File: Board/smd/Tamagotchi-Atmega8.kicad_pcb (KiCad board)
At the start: 2 copper layers, 47.8 x 47.8 mm, 27 parts, among them J1 Conn_02x05_Odd_Even, J2 Conn_01x02, J3 Conn_01x04, J4 Conn_01x07, J5 Conn_01x02, Q1 Q_NPN_BEC, SW1 SW_Push, U1 AMS1117, U2 ATmega328-AU, U3 DS1307Z+, X1 8MHz, X2 32768kHz

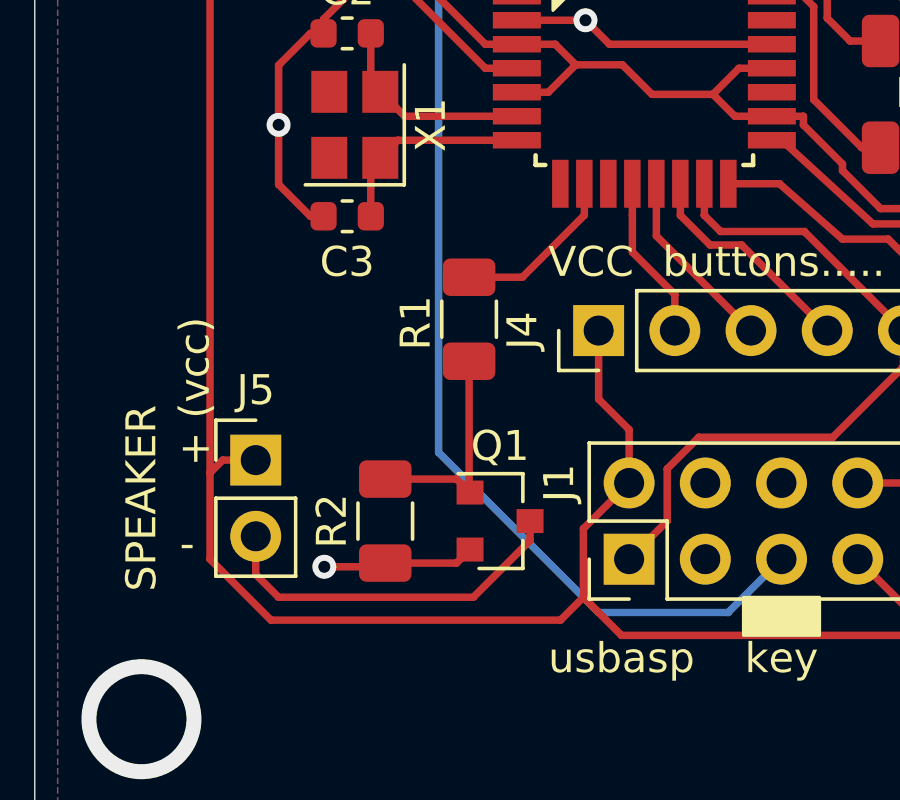
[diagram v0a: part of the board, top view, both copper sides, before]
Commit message: fixed buttons polarity (pull-up state and negative activation)
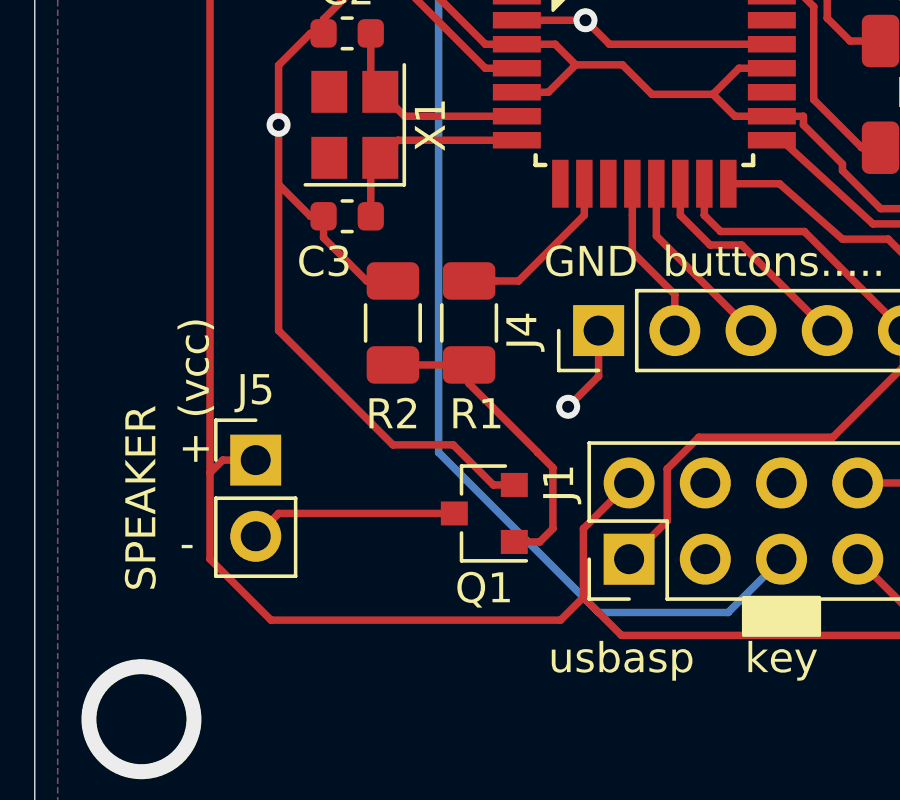
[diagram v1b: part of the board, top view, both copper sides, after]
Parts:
- moved R2 6.61 mm to (118.9, 94.7), turned to 90 degrees
- moved Q1 0.58 mm to (121.9, 101.1), turned to 180 degrees
- moved R1 0.12 mm to (121.4, 94.7)
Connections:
- J4 pad 1: VCC -> GND
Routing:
- net GND: track 90.1 -> 106.4 mm
- net VCC: track 183.7 -> 178.2 mm
- net Net-(J5-Pad2): track 12.2 -> 6.94 mm
- net Net-(Q1-Pad1): track 7.40 -> 10.6 mm
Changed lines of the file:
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@@
     (thickness 1.6)
     (drawings 22)
-    (tracks 258)
+    (tracks 263)
     (zones 0)
     (modules 27)
@@
       (net 16 "Net-(J4-Pad2)"))
     (pad 1 thru_hole rect (at 0 0 90) (size 1.7 1.7) (drill 1) (layers *.Cu *.Mask)
-      (net 2 VCC))
+      (net 1 GND))
     (model ${KISYS3DMOD}/Connector_PinHeader_2.54mm.3dshapes/PinHeader_1x07_P2.54mm_Vertical.wrl
       (at (xyz 0 0 0))
@@
   )
   (module Resistor_SMD:R_1206_3216Metric (layer F.Cu)
-    (at 118.618 101.346 270)
+    (at 118.872 94.742 90)
     (descr "Resistor SMD 1206 (3216 Metric), square (rectangular) end terminal, IPC_7351 nominal, (Body size source: http://www.tortai-tech.com/upload/download/2011102023233369053.pdf), generated with kicad-footprint-generator")
     (tags resistor)
     (attr smd)
-    (fp_text reference R2 (at 0 1.778 90) (layer F.SilkS)
+    (fp_text reference R2 (at -3.048 0 180) (layer F.SilkS)
       (effects (font (size 1 1) (thickness 0.15)))
     )
@@
     (fp_line (start -1.6 -0.8) (end 1.6 -0.8) (layer F.Fab) (width 0.1))
     (fp_line (start -1.6 0.8) (end -1.6 -0.8) (layer F.Fab) (width 0.1))
-    (pad 2 smd roundrect (at 1.4 0 270) (size 1.25 1.75) (layers F.Cu F.Paste F.Mask) (roundrect_rratio 0.2)
-      (net 1 GND))
-    (pad 1 smd roundrect (at -1.4 0 270) (size 1.25 1.75) (layers F.Cu F.Paste F.Mask) (roundrect_rratio 0.2)
+    (pad 2 smd roundrect (at 1.4 0 90) (size 1.25 1.75) (layers F.Cu F.Paste F.Mask) (roundrect_rratio 0.2)
+      (net 1 GND))
+    (pad 1 smd roundrect (at -1.4 0 90) (size 1.25 1.75) (layers F.Cu F.Paste F.Mask) (roundrect_rratio 0.2)
       (net 21 "Net-(Q1-Pad1)"))
     (model ${KISYS3DMOD}/Resistor_SMD.3dshapes/R_1206_3216Metric.wrl
@@
   )
   (module Resistor_SMD:R_1206_3216Metric (layer F.Cu)
-    (at 121.412 94.618 270)
+    (at 121.412 94.742 270)
     (descr "Resistor SMD 1206 (3216 Metric), square (rectangular) end terminal, IPC_7351 nominal, (Body size source: http://www.tortai-tech.com/upload/download/2011102023233369053.pdf), generated with kicad-footprint-generator")
     (tags resistor)
     (attr smd)
-    (fp_text reference R1 (at 0.124 1.778 90) (layer F.SilkS)
+    (fp_text reference R1 (at 3.048 -0.254 180) (layer F.SilkS)
       (effects (font (size 1 1) (thickness 0.15)))
     )
@@
   )
   (module Package_TO_SOT_SMD:SOT-23 (layer F.Cu)
-    (at 122.444 101.346)
+    (at 121.92 101.092 180)
     (descr "SOT-23, Standard")
     (tags SOT-23)
@@
       (effects (font (size 0.5 0.5) (thickness 0.075)))
     )
-    (pad 3 smd rect (at 1 0) (size 0.9 0.8) (layers F.Cu F.Paste F.Mask)
+    (pad 3 smd rect (at 1 0 180) (size 0.9 0.8) (layers F.Cu F.Paste F.Mask)
       (net 17 "Net-(J5-Pad2)"))
-    (pad 2 smd rect (at -1 0.95) (size 0.9 0.8) (layers F.Cu F.Paste F.Mask)
-      (net 1 GND))
-    (pad 1 smd rect (at -1 -0.95) (size 0.9 0.8) (layers F.Cu F.Paste F.Mask)
+    (pad 2 smd rect (at -1 0.95 180) (size 0.9 0.8) (layers F.Cu F.Paste F.Mask)
+      (net 1 GND))
+    (pad 1 smd rect (at -1 -0.95 180) (size 0.9 0.8) (layers F.Cu F.Paste F.Mask)
       (net 21 "Net-(Q1-Pad1)"))
     (model ${KISYS3DMOD}/Package_TO_SOT_SMD.3dshapes/SOT-23.wrl
@@
     (tags capacitor)
     (attr smd)
-    (fp_text reference C3 (at 0 1.524) (layer F.SilkS)
+    (fp_text reference C3 (at -0.762 1.524) (layer F.SilkS)
       (effects (font (size 1 1) (thickness 0.15)))
     )
@@
     (effects (font (size 1 1) (thickness 0.15)))
   )
-  (gr_text VCC (at 125.476 92.71) (layer F.SilkS)
+  (gr_text GND (at 125.476 92.71) (layer F.SilkS)
     (effects (font (size 1 1) (thickness 0.15)))
   )
@@
   (via (at 110.49 107.95) (size 4) (drill 3) (layers F.Cu B.Cu) (net 1))
   (via (at 110.49 67.31) (size 4) (drill 3) (layers F.Cu B.Cu) (net 1))
-  (segment (start 120.994 102.746) (end 121.444 102.296) (width 0.25) (layer F.Cu) (net 1))
-  (segment (start 118.618 102.746) (end 120.994 102.746) (width 0.25) (layer F.Cu) (net 1))
   (segment (start 147.658 70.358) (end 146.558 70.358) (width 0.25) (layer F.Cu) (net 1))
   (segment (start 148.59 80.264) (end 148.59 71.29) (width 0.25) (layer F.Cu) (net 1))
@@
   (segment (start 125.292 84.652) (end 125.292 84.652) (width 0.25) (layer F.Cu) (net 1))
   (via (at 125.292 84.652) (size 0.8) (drill 0.4) (layers F.Cu B.Cu) (net 1))
-  (via (at 116.586 102.87) (size 0.8) (drill 0.4) (layers F.Cu B.Cu) (net 1))
+  (via (at 124.714 97.536) (size 0.8) (drill 0.4) (layers F.Cu B.Cu) (net 1))
   (segment (start 144.866 96.688) (end 144.866 101.578) (width 0.25) (layer F.Cu) (net 1))
   (via (at 144.866 101.6) (size 0.8) (drill 0.4) (layers F.Cu B.Cu) (net 1))
@@
   (via (at 129.794 76.962) (size 0.8) (drill 0.4) (layers F.Cu B.Cu) (net 1))
   (segment (start 128.548 78.359) (end 129.794 77.113) (width 0.25) (layer F.Cu) (net 1))
-  (segment (start 118.494 102.87) (end 118.618 102.746) (width 0.25) (layer F.Cu) (net 1))
-  (segment (start 116.586 102.87) (end 118.494 102.87) (width 0.25) (layer F.Cu) (net 1))
+  (segment (start 117.997 93.342) (end 118.872 93.342) (width 0.25) (layer F.Cu) (net 1))
+  (segment (start 116.5605 91.9055) (end 117.997 93.342) (width 0.25) (layer F.Cu) (net 1))
+  (segment (start 116.5605 91.186) (end 116.5605 91.9055) (width 0.25) (layer F.Cu) (net 1))
+  (segment (start 122.22 100.142) (end 120.884 98.806) (width 0.25) (layer F.Cu) (net 1))
+  (segment (start 122.92 100.142) (end 122.22 100.142) (width 0.25) (layer F.Cu) (net 1))
+  (segment (start 120.884 98.806) (end 118.872 98.806) (width 0.25) (layer F.Cu) (net 1))
+  (segment (start 115.062 94.996) (end 115.062 90.125) (width 0.25) (layer F.Cu) (net 1))
+  (segment (start 118.872 98.806) (end 115.062 94.996) (width 0.25) (layer F.Cu) (net 1))
+  (segment (start 125.73 96.52) (end 124.714 97.536) (width 0.25) (layer F.Cu) (net 1))
+  (segment (start 125.73 94.996) (end 125.73 96.52) (width 0.25) (layer F.Cu) (net 1))
   (segment (start 136.646 72.898) (end 136.652 72.892) (width 0.25) (layer F.Cu) (net 2))
   (segment (start 149.266 101.006) (end 149.18 101.092) (width 0.25) (layer F.Cu) (net 2))
@@
   (segment (start 148.59 105.156) (end 149.255001 104.490999) (width 0.25) (layer F.Cu) (net 2))
   (segment (start 123.004 85.452) (end 121.954 85.452) (width 0.25) (layer F.Cu) (net 2))
-  (segment (start 126.746 100.076) (end 126.746 98.298) (width 0.25) (layer F.Cu) (net 2))
-  (segment (start 125.73 97.282) (end 125.73 94.996) (width 0.25) (layer F.Cu) (net 2))
-  (segment (start 126.746 98.298) (end 125.73 97.282) (width 0.25) (layer F.Cu) (net 2))
   (segment (start 141.63 98.942) (end 141.63 101.092) (width 0.25) (layer F.Cu) (net 2))
   (segment (start 132.556 87.852) (end 132.556 88.14119) (width 0.25) (layer F.Cu) (net 2))
@@
   (segment (start 128.27 93.793919) (end 126.854 92.377919) (width 0.25) (layer F.Cu) (net 16))
   (segment (start 128.27 94.996) (end 128.27 93.793919) (width 0.25) (layer F.Cu) (net 16))
-  (segment (start 115.062 103.886) (end 114.3 103.124) (width 0.25) (layer F.Cu) (net 17))
-  (segment (start 121.554 103.886) (end 115.062 103.886) (width 0.25) (layer F.Cu) (net 17))
-  (segment (start 114.3 103.124) (end 114.3 101.854) (width 0.25) (layer F.Cu) (net 17))
-  (segment (start 123.444 101.346) (end 123.444 101.996) (width 0.25) (layer F.Cu) (net 17))
-  (segment (start 123.444 101.996) (end 121.554 103.886) (width 0.25) (layer F.Cu) (net 17))
+  (segment (start 115.062 101.092) (end 114.3 101.854) (width 0.25) (layer F.Cu) (net 17))
+  (segment (start 120.92 101.092) (end 115.062 101.092) (width 0.25) (layer F.Cu) (net 17))
   (segment (start 139.44 88.9) (end 140.202 89.662) (width 0.25) (layer F.Cu) (net 18))
   (segment (start 137.928 88.9) (end 139.44 88.9) (width 0.25) (layer F.Cu) (net 18))
@@
   (segment (start 139.44 81.788) (end 140.202 81.026) (width 0.25) (layer F.Cu) (net 20))
   (segment (start 137.922 81.788) (end 139.44 81.788) (width 0.25) (layer F.Cu) (net 20))
-  (segment (start 121.412 100.364) (end 121.444 100.396) (width 0.25) (layer F.Cu) (net 21))
-  (segment (start 121.412 96.018) (end 121.412 100.364) (width 0.25) (layer F.Cu) (net 21))
-  (segment (start 120.994 99.946) (end 121.444 100.396) (width 0.25) (layer F.Cu) (net 21))
-  (segment (start 118.618 99.946) (end 120.994 99.946) (width 0.25) (layer F.Cu) (net 21))
-  (segment (start 125.254 91.152) (end 125.254 90.102) (width 0.25) (layer F.Cu) (net 22))
-  (segment (start 123.188 93.218) (end 125.254 91.152) (width 0.25) (layer F.Cu) (net 22))
-  (segment (start 121.412 93.218) (end 123.188 93.218) (width 0.25) (layer F.Cu) (net 22))
+  (segment (start 118.872 96.142) (end 121.412 96.142) (width 0.25) (layer F.Cu) (net 21))
+  (segment (start 123.764 102.042) (end 122.92 102.042) (width 0.25) (layer F.Cu) (net 21))
+  (segment (start 124.206 101.6) (end 123.764 102.042) (width 0.25) (layer F.Cu) (net 21))
+  (segment (start 121.412 96.767) (end 123.695001 99.050001) (width 0.25) (layer F.Cu) (net 21))
+  (segment (start 123.695001 99.050001) (end 123.695001 99.057001) (width 0.25) (layer F.Cu) (net 21))
+  (segment (start 124.206 99.568) (end 124.206 101.6) (width 0.25) (layer F.Cu) (net 21))
+  (segment (start 121.412 96.142) (end 121.412 96.767) (width 0.25) (layer F.Cu) (net 21))
+  (segment (start 123.695001 99.057001) (end 124.206 99.568) (width 0.25) (layer F.Cu) (net 21))
+  (segment (start 123.064 93.342) (end 122.287 93.342) (width 0.25) (layer F.Cu) (net 22))
+  (segment (start 125.254 91.152) (end 123.064 93.342) (width 0.25) (layer F.Cu) (net 22))
+  (segment (start 122.287 93.342) (end 121.412 93.342) (width 0.25) (layer F.Cu) (net 22))
+  (segment (start 125.254 90.102) (end 125.254 91.152) (width 0.25) (layer F.Cu) (net 22))
   (segment (start 134.503 88.9) (end 135.128 88.9) (width 0.25) (layer F.Cu) (net 23))
   (segment (start 132.89999 87.29699) (end 134.503 88.9) (width 0.25) (layer F.Cu) (net 23))
